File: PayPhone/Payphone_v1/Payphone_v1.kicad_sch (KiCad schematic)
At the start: 86 parts, among them J1 JST_05, J2 Molex_26-60-4030, J3 Molex_26-60-4040, J6 PINHD_1x5_Male, J7 PINHD_1x2_Male, J8 PINHD_1x2_Male, J9 PINHD_1x2_Male, K1 G6S-2, Q1 2N7002, Q2 MMBT3904, Q3 STN4NF20L, Q4 2N7002, Q5 MMBT3906, U1 MCP23008-E/SO, U2 MC34063ADR2G, U3 UC3843BD1R2G, U4 ADS1115IDGS

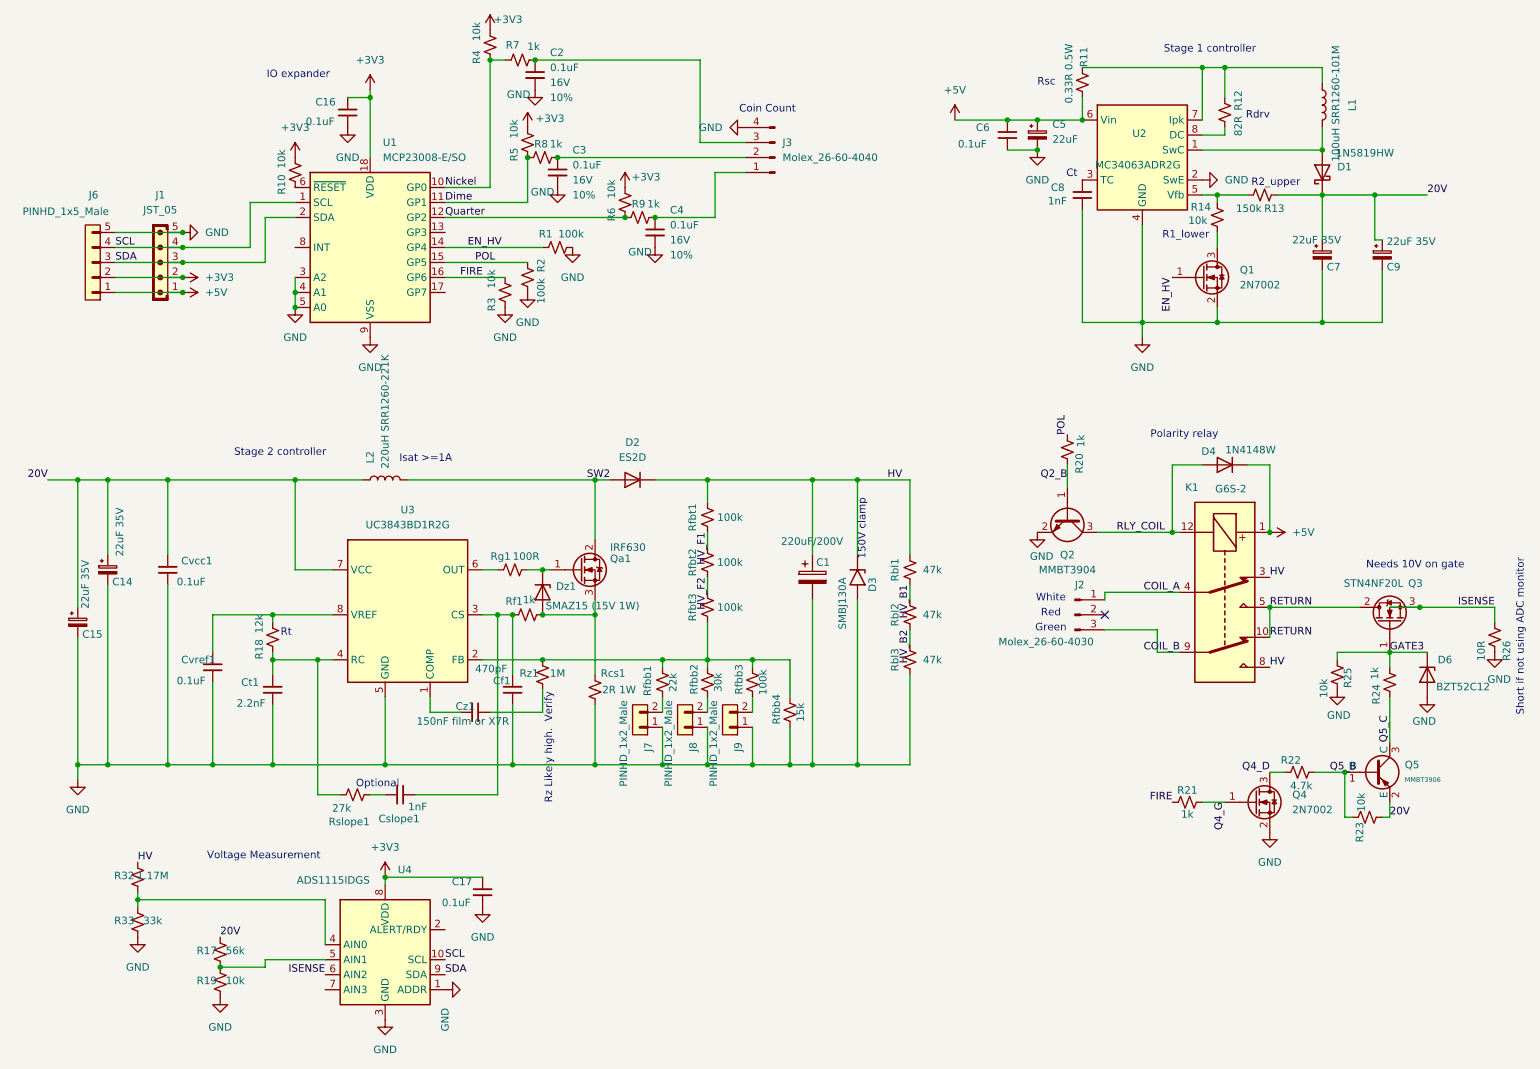
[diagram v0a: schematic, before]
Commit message: Payphone coin board: parts placed in groups with routing notes; HV indicator LED (D7, lights above 24 V); +3V3 renamed VIO (host's I2C logic level) with JP1 VIO=5V; green debug LEDs for the coin lines and EN_HV/POL/FIRE; Rbl1-3 1M
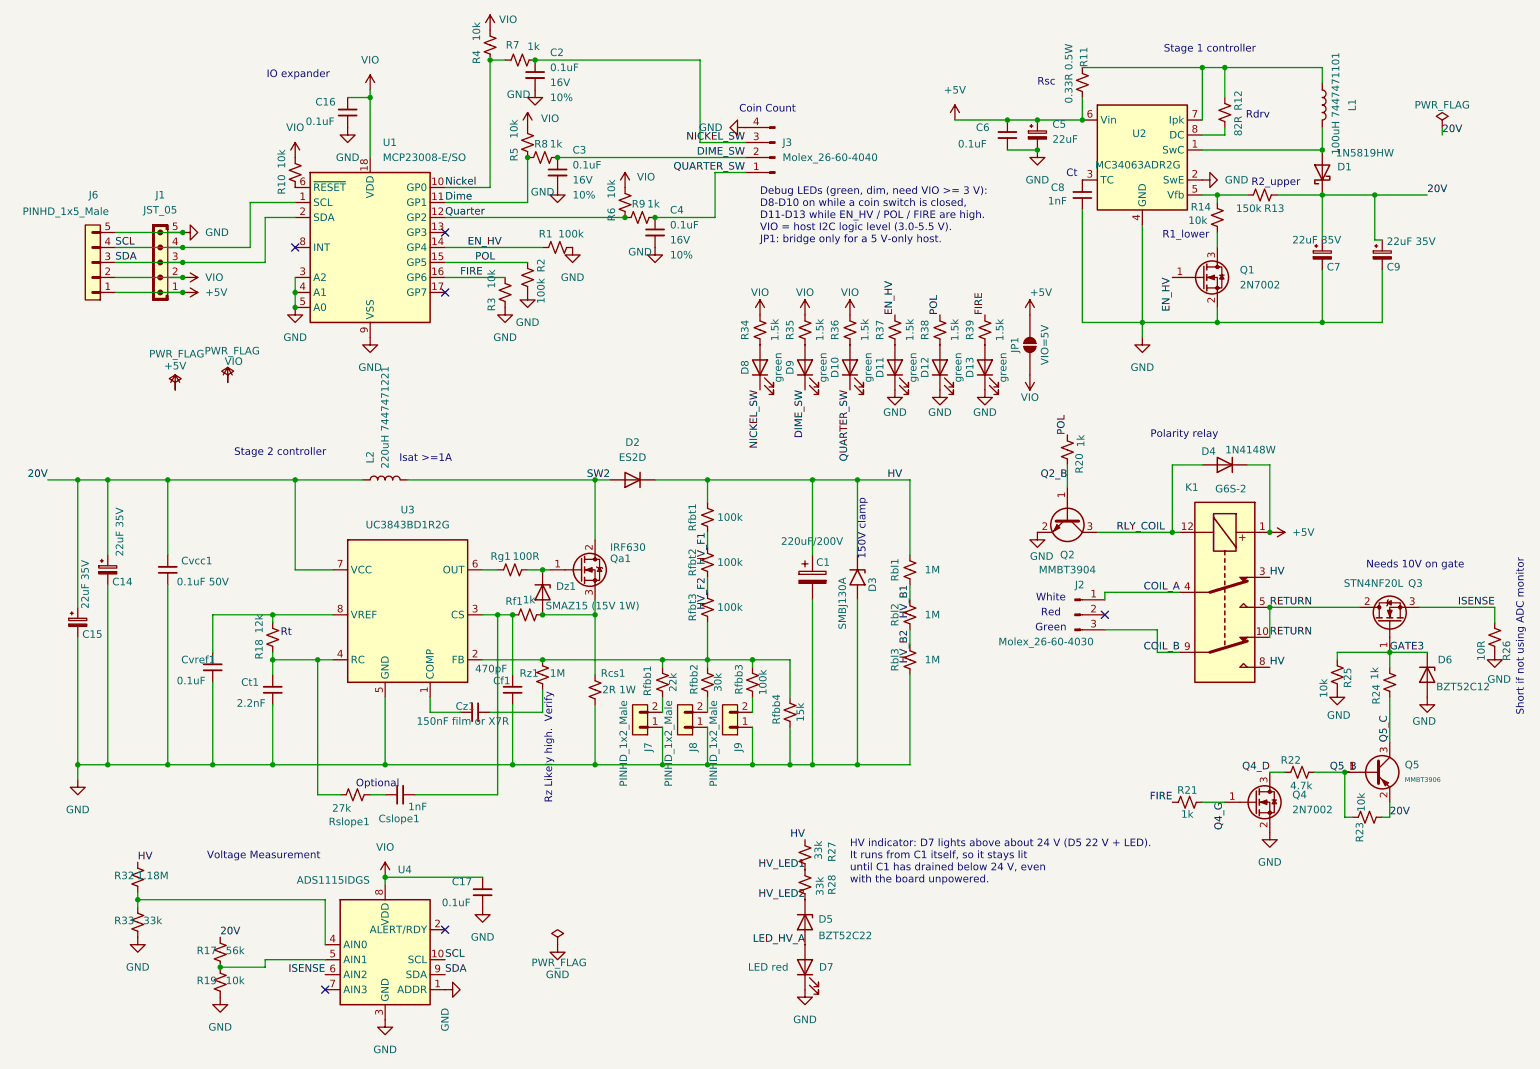
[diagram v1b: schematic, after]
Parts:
- added D10, D11, D12, D13, D8, D9: green, LED_SMD:LED_0805_2012Metric, symbol Device:LED
- added D5: BZT52C22, Diode_SMD:D_SOD-123, symbol Device:D_Zener
- added D7: LED red, LED_SMD:LED_0805_2012Metric, symbol Device:LED
- added JP1: VIO=5V, Jumper:SolderJumper-2_P1.3mm_Open_RoundedPad1.0x1.5mm, symbol Jumper:SolderJumper_2_Open
- added R27, R28: 33k, Resistor_SMD:R_1206_3216Metric, symbol PCM_SparkFun-Resistor:R_Small
- added R34, R35, R36, R37, R38, R39: 1.5k, Resistor_SMD:R_0805_2012Metric, symbol PCM_SparkFun-Resistor:R_Small
- C14, C15, C5, C7, C9: footprint Capacitor_SMD:CP_Elec_6.3x5.4 -> Capacitor_THT:CP_Radial_D5.0mm_P2.00mm
- Cvcc1: value 0.1uF -> 0.1uF 50V
- L1: value 100uH SRR1260-101M -> 100uH 7447471101; footprint Inductor_SMD:L_Bourns_SRR1260 -> Inductor_THT:L_Radial_D12.0mm_P5.00mm_Fastron_11P
- L2: value 220uH SRR1260-221K -> 220uH 7447471221; footprint Inductor_SMD:L_Bourns_SRR1260 -> Inductor_THT:L_Radial_D12.0mm_P5.00mm_Fastron_11P
- Q5: symbol PCM_JLCPCB-Transistors:PNP,MMBT3906 -> Transistor_BJT:MMBT3906
- R32: value 1.17M -> 1.18M
- Rbl1, Rbl2, Rbl3: value 47k -> 1M
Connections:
- net +5V: now also JP1.2 (B)
- net EN_HV: now also R37.2
- net FIRE: now also R39.2
- net GND: now also D11.1 (K), D12.1 (K), D13.1 (K), D7.1 (K)
- net HV: now also R27.2
- net POL: now also R38.2
- net DIME_SW: now reaches C3.1, J3.2 (Pin_2), R8.1
- net DIME_SW: now also D9.1 (K)
- net QUARTER_SW: now reaches C4.1, J3.1 (Pin_1), R9.1
- net QUARTER_SW: now also D10.1 (K)
- net NICKEL_SW: now reaches C2.1, J3.3 (Pin_3), R7.1
- net NICKEL_SW: now also D8.1 (K)
- net +3V3 renamed VIO
- net VIO: now also JP1.1 (A), R34.2, R35.2, R36.2
- new net: D9.2 (A), R35.1
- new net: D8.2 (A), R34.1
- new net: D11.2 (A), R37.1
- new net: D13.2 (A), R39.1
- new net: D10.2 (A), R36.1
- new net: D12.2 (A), R38.1
- new net HV_LED1: R27.1, R28.2
- new net HV_LED2: D5.1 (K), R28.1
- new net LED_HV_A: D5.2 (A), D7.2 (A)
- no-connect marks 1 -> 6
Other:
- note added: "Debug LEDs (green, dim, need VIO >= 3 V): D8-D10 on while a coin switch is closed, D11-D13 while EN_HV / POL / FIRE are high. VIO = host I2C logic level (3.0-5.5 V). JP1: bridge only for a 5 V-only host."
- note added: "HV indicator: D7 lights above about 24 V (D5 22 V + LED). It runs from C1 itself, so it stays lit until C1 has drained below 24 V, even with the board unpowered."
